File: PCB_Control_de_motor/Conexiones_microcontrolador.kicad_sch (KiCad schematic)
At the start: 17 parts, among them SW1 SSSF021500, U1 ESP32-S3-WROOM-1

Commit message: Esquemático listo
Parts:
- added C3: 22uF, PCM_JLCPCB:C_0805, symbol PCM_JLCPCB-Capacitors:0805,22uF
- added IC1: USBLC6-2SC6, SamacSys_Parts:SOT95P280X145-6N, symbol SamacSys_Parts:USBLC6-2SC6
- renumbered C3 to C4, C4 to C5, C5 to C6, C6 to C7, R6 to R10, R7 to R11, R1 to R5, R2 to R6, R3 to R7, R4 to R8, R5 to R9
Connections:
- net GND: now also C3.2, IC1.2 (GND)
- net V_USB: now also C3.1, IC1.5 (VBUS)
- net at USB-C1.A7 (D-_1), USB-C1.B7 (D-_2): now also IC1.3 (I/O2_1); no longer C7.1, R10.1
- net at USB-C1.A6 (D+_1), USB-C1.B6 (D+_2): now also IC1.1 (I/O1_1); no longer C6.1, R9.1
- new net: C7.1, IC1.6 (I/O1_2), R9.1
- new net: C6.1, IC1.4 (I/O2_2), R10.1
- no-connect marks 21 -> 43
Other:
- moved on the sheet: C6, C7, R10, R5, R8, R9, USB-C1

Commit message: Corrección de la huella del ESP32
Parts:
- removed U1: ESP32-S3-WROOM-1, RF_Module:ESP32-S3-WROOM-1, symbol RF_Module:ESP32-S3-WROOM-1
- added IC4: ESP32-S3-WROOM-1-N16, SamacSys_Parts:ESP32S3WROOM1N16, symbol SamacSys_Parts:ESP32-S3-WROOM-1-N16
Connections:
- net +3.3V: now also IC4.2 (3V3)
- net ADC: now also IC4.39 (IO1)
- net BOOT0: now also IC4.27 (IO0)
- net BOTON: now also IC4.38 (IO2)
- net EN_ESP32: now also IC4.3 (EN)
- net GND: now also IC4.1 (GND_1), IC4.34 (IO41), IC4.40 (GND_2), IC4.41 (GND_3), IC4.42 (GND_4), IC4.43 (GND_5), IC4.44 (GND_6), IC4.45 (GND_7), IC4.46 (GND_8), IC4.47 (GND_9), IC4.48 (GND_10), IC4.49 (GND_11)
- net LSA: now also IC4.30 (IO37)
- net LSC: now also IC4.31 (IO38)
- net PWM_1: now also IC4.4 (IO4)
- net PWM_2: now also IC4.5 (IO5)
- net USB_D+: now also IC4.22 (IO14)
- net USB_D-: now also IC4.21 (IO13)

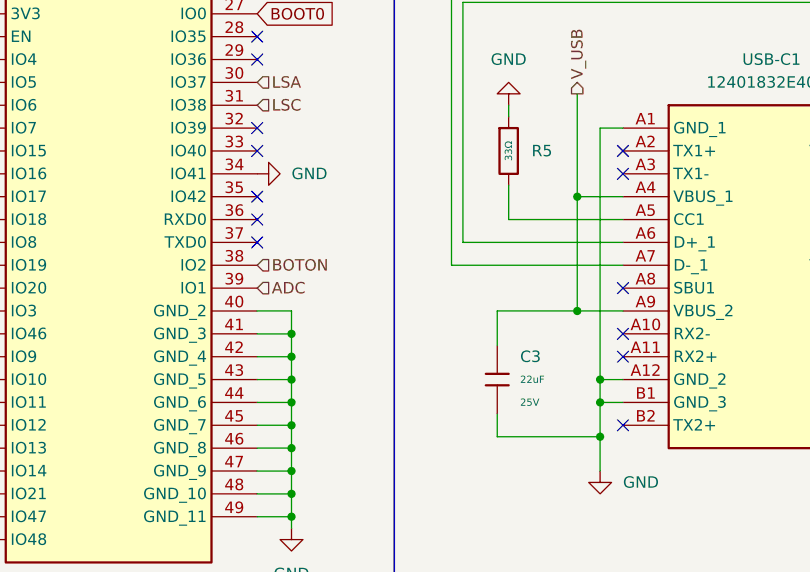
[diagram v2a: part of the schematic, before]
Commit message: Corrección 2 del esquemático
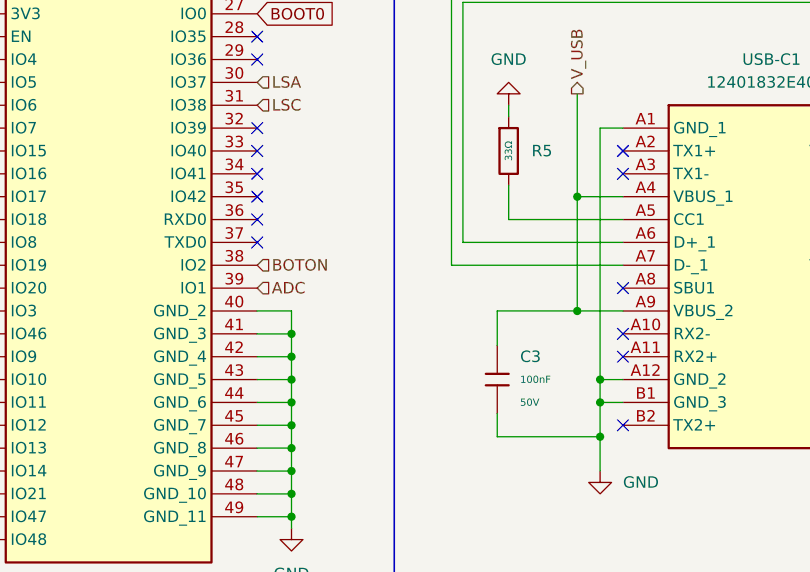
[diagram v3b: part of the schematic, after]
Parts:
- removed C3: 22uF, PCM_JLCPCB:C_0805, symbol PCM_JLCPCB-Capacitors:0805,22uF
- added C3: 100nF, PCM_JLCPCB:C_0603, symbol PCM_JLCPCB-Capacitors:0603,100nF
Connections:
- net GND: now also C3.2; no longer IC4.34 (IO41)
- net V_USB: now also C3.1
- no-connect marks 43 -> 44
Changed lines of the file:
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@@
 	)
 	(no_connect
+		(at 71.12 52.07)
+	)
+	(no_connect
 		(at 38.1 69.85)
 	)
@@
 	)
 	(symbol
+		(lib_id "PCM_JLCPCB-Capacitors:0603,100nF")
+		(at 97.79 74.93 0)
+		(unit 1)
+		(exclude_from_sim no)
+		(in_bom yes)
+		(on_board yes)
+		(dnp no)
+		(fields_autoplaced yes)
+		(property "Reference" "C3"
+			(at 100.33 72.3899 0)
+			(effects
+				(font
+					(size 1.27 1.27)
+				)
+				(justify left)
+			)
+		)
+		(property "Value" "100nF"
+			(at 100.33 74.93 0)
+			(effects
+				(font
+					(size 0.8 0.8)
+				)
+				(justify left)
+			)
+		)
+		(property "Footprint" "PCM_JLCPCB:C_0603"
+			(at 96.012 74.93 90)
+			(effects
+				(font
+					(size 1.27 1.27)
+				)
+				(hide yes)
+			)
+		)
+		(property "Datasheet" "https://www.lcsc.com/datasheet/lcsc_datasheet_2211101700_YAGEO-CC0603KRX7R9BB104_C14663.pdf"
+			(at 97.79 74.93 0)
+			(effects
+				(font
+					(size 1.27 1.27)
+				)
+				(hide yes)
+			)
+		)
+		(property "Description" "50V 100nF X7R ±10% 0603 Multilayer Ceramic Capacitors MLCC - SMD/SMT ROHS"
+			(at 97.79 74.93 0)
+			(effects
+				(font
+					(size 1.27 1.27)
+				)
+				(hide yes)
+			)
+		)
+		(property "LCSC" "C14663"
+			(at 97.79 74.93 0)
+			(effects
+				(font
+					(size 1.27 1.27)
+				)
+				(hide yes)
+			)
+		)
+		(property "Stock" "66445262"
+			(at 97.79 74.93 0)
+			(effects
+				(font
+					(size 1.27 1.27)
+				)
+				(hide yes)
+			)
+		)
+		(property "Price" "0.006USD"
+			(at 97.79 74.93 0)
+			(effects
+				(font
+					(size 1.27 1.27)
+				)
+				(hide yes)
+			)
+		)
+		(property "Process" "SMT"
+			(at 97.79 74.93 0)
+			(effects
+				(font
+					(size 1.27 1.27)
+				)
+				(hide yes)
+			)
+		)
+		(property "Minimum Qty" "20"
+			(at 97.79 74.93 0)
+			(effects
+				(font
+					(size 1.27 1.27)
+				)
+				(hide yes)
+			)
+		)
+		(property "Attrition Qty" "10"
+			(at 97.79 74.93 0)
+			(effects
+				(font
+					(size 1.27 1.27)
+				)
+				(hide yes)
+			)
+		)
+		(property "Class" "Basic Component"
+			(at 97.79 74.93 0)
+			(effects
+				(font
+					(size 1.27 1.27)
+				)
+				(hide yes)
+			)
+		)
+		(property "Category" "Capacitors,Multilayer Ceramic Capacitors MLCC - SMD/SMT"
+			(at 97.79 74.93 0)
+			(effects
+				(font
+					(size 1.27 1.27)
+				)
+				(hide yes)
+			)
+		)
+		(property "Manufacturer" "YAGEO"
+			(at 97.79 74.93 0)
+			(effects
+				(font
+					(size 1.27 1.27)
+				)
+				(hide yes)
+			)
+		)
+		(property "Part" "CC0603KRX7R9BB104"
+			(at 97.79 74.93 0)
+			(effects
+				(font
+					(size 1.27 1.27)
+				)
+				(hide yes)
+			)
+		)
+		(property "Voltage Rated" "50V"
+			(at 100.33 77.47 0)
+			(effects
+				(font
+					(size 0.8 0.8)
+				)
+				(justify left)
+			)
+		)
+		(property "Tolerance" "±10%"
+			(at 97.79 74.93 0)
+			(effects
+				(font
+					(size 1.27 1.27)
+				)
+				(hide yes)
+			)
+		)
+		(property "Capacitance" "100nF"
+			(at 97.79 74.93 0)
+			(effects
+				(font
+					(size 1.27 1.27)
+				)
+				(hide yes)
+			)
+		)
+		(property "Temperature Coefficient" "X7R"
+			(at 97.79 74.93 0)
+			(effects
+				(font
+					(size 1.27 1.27)
+				)
+				(hide yes)
+			)
+		)
+		(pin "1"
+		)
+		(pin "2"
+		)
+		(instances
+			(project ""
+				(path "/8d17a2c0-3da6-4d80-8f2f-d7746ccde60e/17d37bd9-22de-4c8a-b60d-bd9473156cba"
+					(reference "C3")
+					(unit 1)
+				)
+			)
+		)
+	)
+	(symbol
 		(lib_id "PCM_JLCPCB-Resistors:0402,0Ω")
 		(at 120.65 138.43 0)
@@
 	)
 	(symbol
-		(lib_id "PCM_JLCPCB-Capacitors:0805,22uF")
-		(at 97.79 74.93 0)
-		(unit 1)
-		(exclude_from_sim no)
-		(in_bom yes)
-		(on_board yes)
-		(dnp no)
-		(fields_autoplaced yes)
-		(property "Reference" "C3"
-			(at 100.33 72.3899 0)
-			(effects
-				(font
-					(size 1.27 1.27)
-				)
-				(justify left)
-			)
-		)
-		(property "Value" "22uF"
-			(at 100.33 74.93 0)
-			(effects
-				(font
-					(size 0.8 0.8)
-				)
-				(justify left)
-			)
-		)
-		(property "Footprint" "PCM_JLCPCB:C_0805"
-			(at 96.012 74.93 90)
-			(effects
-				(font
-					(size 1.27 1.27)
-				)
-				(hide yes)
-			)
-		)
-		(property "Datasheet" "https://www.lcsc.com/datasheet/lcsc_datasheet_2304140030_Samsung-Electro-Mechanics-CL21A226MAQNNNE_C45783.pdf"
-			(at 97.79 74.93 0)
-			(effects
-				(font
-					(size 1.27 1.27)
-				)
-				(hide yes)
-			)
-		)
-		(property "Description" "25V 22uF X5R ±20% 0805 Multilayer Ceramic Capacitors MLCC - SMD/SMT ROHS"
-			(at 97.79 74.93 0)
-			(effects
-				(font
-					(size 1.27 1.27)
-				)
-				(hide yes)
-			)
-		)
-		(property "LCSC" "C45783"
-			(at 97.79 74.93 0)
-			(effects
-				(font
-					(size 1.27 1.27)
-				)
-				(hide yes)
-			)
-		)
-		(property "Stock" "1873210"
-			(at 97.79 74.93 0)
-			(effects
-				(font
-					(size 1.27 1.27)
-				)
-				(hide yes)
-			)
-		)
-		(property "Price" "0.024USD"
-			(at 97.79 74.93 0)
-			(effects
-				(font
-					(size 1.27 1.27)
-				)
-				(hide yes)
-			)
-		)
-		(property "Process" "SMT"
-			(at 97.79 74.93 0)
-			(effects
-				(font
-					(size 1.27 1.27)
-				)
-				(hide yes)
-			)
-		)
-		(property "Minimum Qty" "20"
-			(at 97.79 74.93 0)
-			(effects
-				(font
-					(size 1.27 1.27)
-				)
-				(hide yes)
-			)
-		)
-		(property "Attrition Qty" "6"
-			(at 97.79 74.93 0)
-			(effects
-				(font
-					(size 1.27 1.27)
-				)
-				(hide yes)
-			)
-		)
-		(property "Class" "Basic Component"
-			(at 97.79 74.93 0)
-			(effects
-				(font
-					(size 1.27 1.27)
-				)
-				(hide yes)
-			)
-		)
-		(property "Category" "Capacitors,Multilayer Ceramic Capacitors MLCC - SMD/SMT"
-			(at 97.79 74.93 0)
-			(effects
-				(font
-					(size 1.27 1.27)
-				)
-				(hide yes)
-			)
-		)
-		(property "Manufacturer" "Samsung Electro-Mechanics"
-			(at 97.79 74.93 0)
-			(effects
-				(font
-					(size 1.27 1.27)
-				)
-				(hide yes)
-			)
-		)
-		(property "Part" "CL21A226MAQNNNE"
-			(at 97.79 74.93 0)
-			(effects
-				(font
-					(size 1.27 1.27)
-				)
-				(hide yes)
-			)
-		)
-		(property "Voltage Rated" "25V"
-			(at 100.33 77.47 0)
-			(effects
-				(font
-					(size 0.8 0.8)
-				)
-				(justify left)
-			)
-		)
-		(property "Tolerance" "±20%"
-			(at 97.79 74.93 0)
-			(effects
-				(font
-					(size 1.27 1.27)
-				)
-				(hide yes)
-			)
-		)
-		(property "Capacitance" "22uF"
-			(at 97.79 74.93 0)
-			(effects
-				(font
-					(size 1.27 1.27)
-				)
-				(hide yes)
-			)
-		)
-		(property "Temperature Coefficient" "X5R"
-			(at 97.79 74.93 0)
-			(effects
-				(font
-					(size 1.27 1.27)
-				)
-				(hide yes)
-			)
-		)
-		(pin "1"
-		)
-		(pin "2"
-		)
-		(instances
-			(project ""
-				(path "/8d17a2c0-3da6-4d80-8f2f-d7746ccde60e/17d37bd9-22de-4c8a-b60d-bd9473156cba"
-					(reference "C3")
-					(unit 1)
-				)
-			)
-		)
-	)
-	(symbol
 		(lib_id "power:+3.3V")
 		(at 41.91 135.89 0)
@@
 					(unit 1)
 				)
-			)
-		)
-	)
-	(symbol
-		(lib_id "power:GND")
-		(at 71.12 52.07 90)
-		(unit 1)
-		(exclude_from_sim no)
-		(in_bom yes)
-		(on_board yes)
-		(dnp no)
-		(fields_autoplaced yes)
-		(property "Reference" "#PWR037"
-			(at 77.47 52.07 0)
-			(effects
-				(font
-					(size 1.27 1.27)
-				)
-				(hide yes)
-			)
-		)
-		(property "Value" "GND"
-			(at 74.93 52.0699 90)
-			(effects
-				(font
-					(size 1.27 1.27)
-				)
-				(justify right)
-			)
-		)
-		(property "Footprint" ""
-			(at 71.12 52.07 0)
-			(effects
-				(font
-					(size 1.27 1.27)
-				)
-				(hide yes)
-			)
-		)
-		(property "Datasheet" ""
-			(at 71.12 52.07 0)
-			(effects
-				(font
-					(size 1.27 1.27)
-				)
-				(hide yes)
-			)
-		)
-		(property "Description" "Power symbol creates a global label with name \"GND\" , ground"
-			(at 71.12 52.07 0)
-			(effects
-				(font
-					(size 1.27 1.27)
-				)
-				(hide yes)
-			)
-		)
-		(pin "1"
-		)
-		(instances
-			(project "PCB_Control_de_motor"
-				(path "/8d17a2c0-3da6-4d80-8f2f-d7746ccde60e/17d37bd9-22de-4c8a-b60d-bd9473156cba"
-					(reference "#PWR037")
-					(unit 1)
-				)

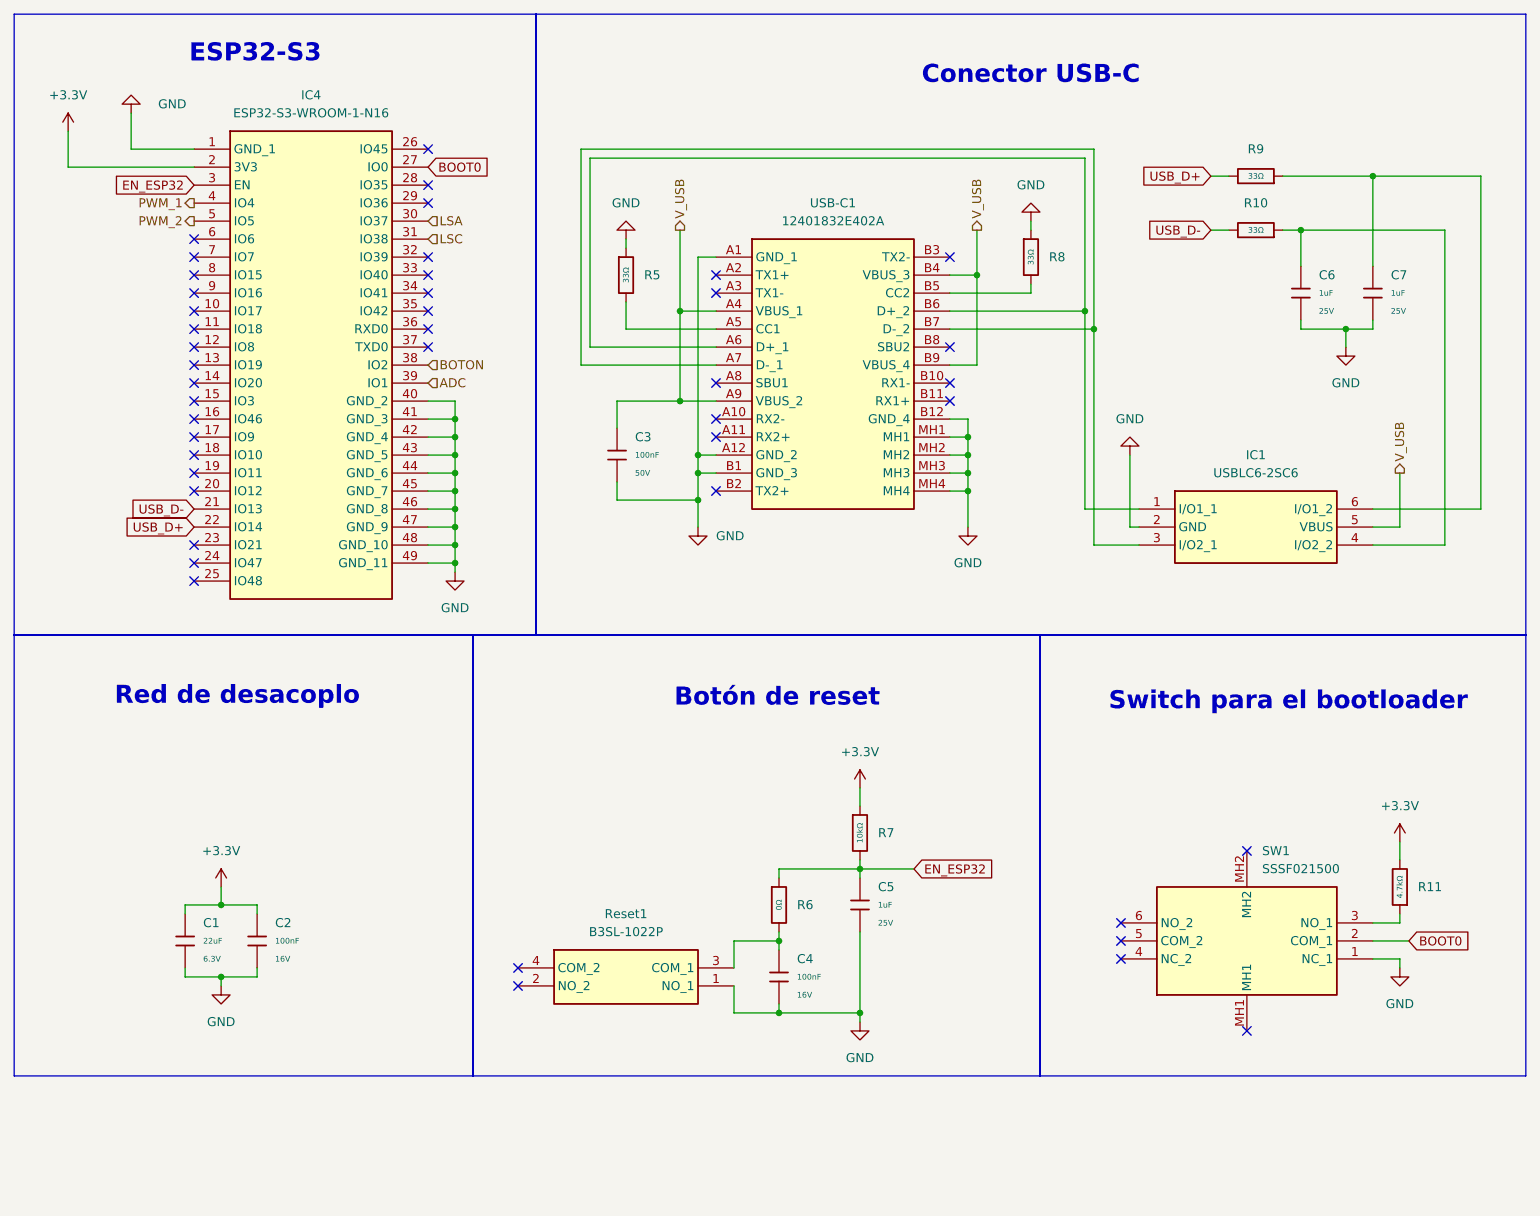
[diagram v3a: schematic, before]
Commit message: Corrección 3 del esquemático
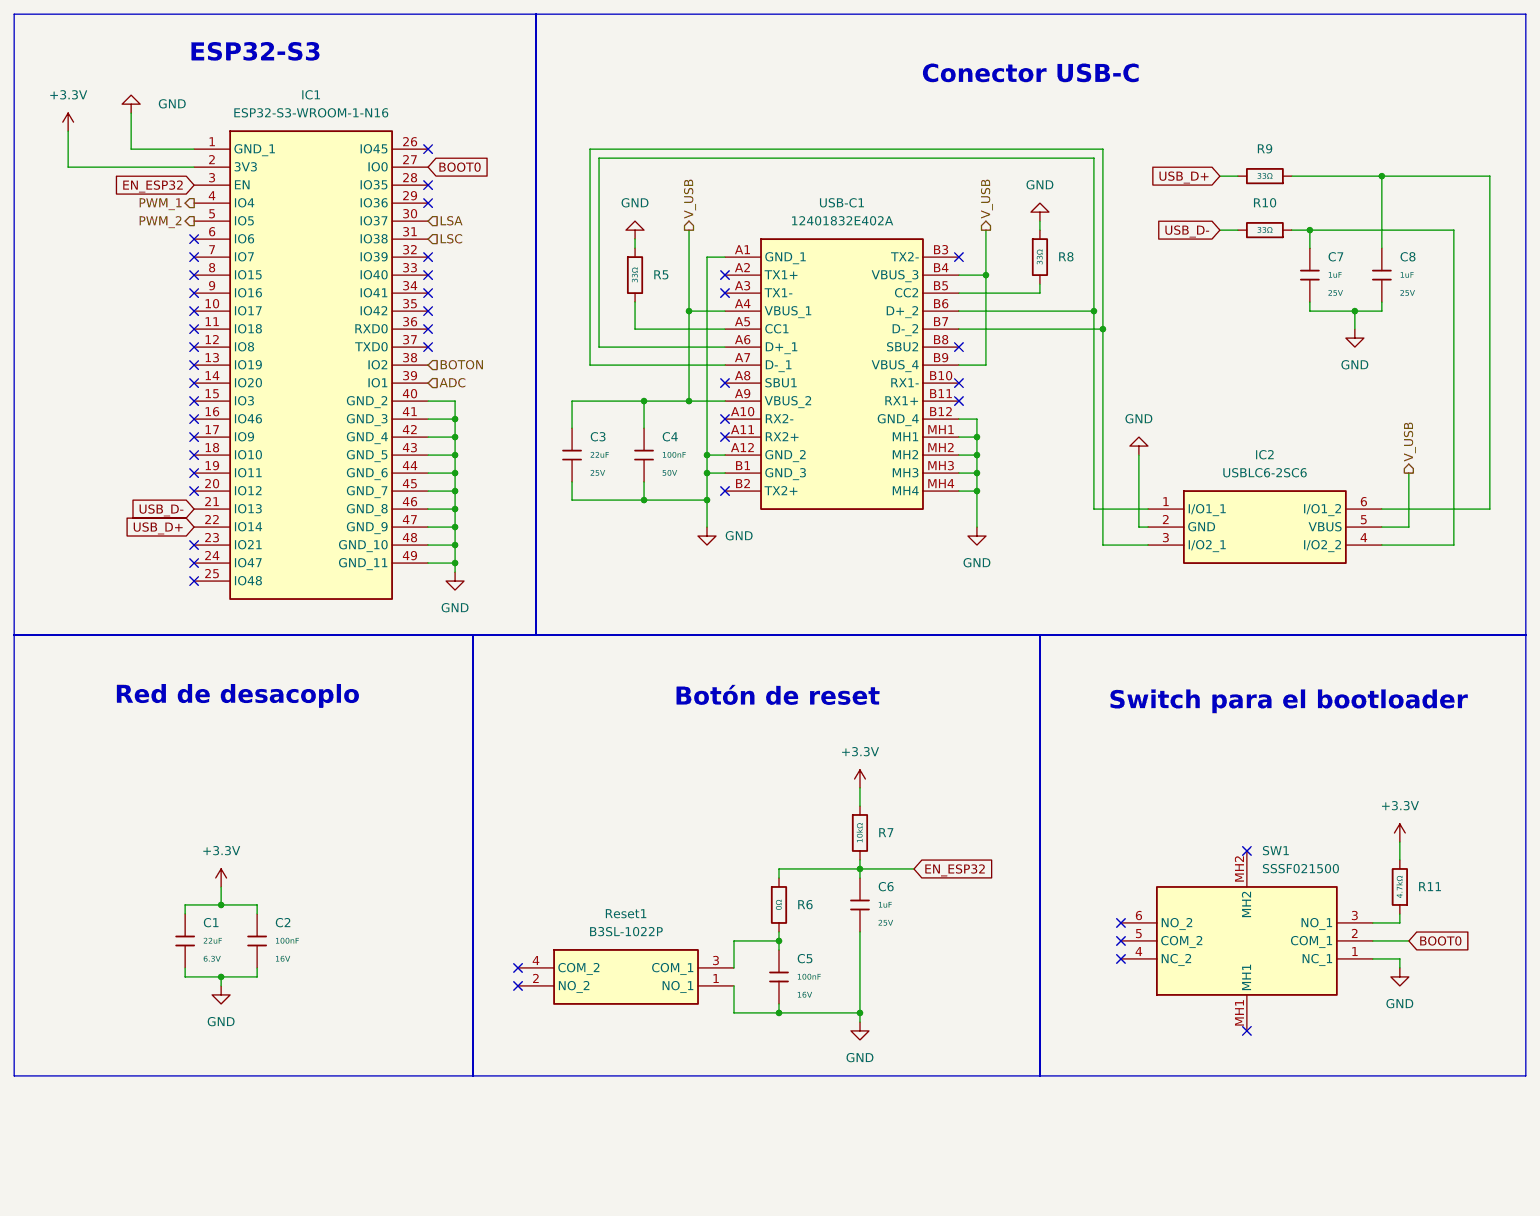
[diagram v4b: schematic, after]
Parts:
- added C3: 22uF, PCM_JLCPCB:C_0805, symbol PCM_JLCPCB-Capacitors:0805,22uF
- renumbered C3 to C4, C4 to C5, C5 to C6, C6 to C7, C7 to C8, IC4 to IC1, IC1 to IC2
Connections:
- net GND: now also C3.2
- net V_USB: now also C3.1
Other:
- moved on the sheet: C4, C7, C8, IC2, R10, R5, R8, R9, USB-C1
